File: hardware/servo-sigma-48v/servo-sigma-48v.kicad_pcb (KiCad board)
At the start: 4 copper layers, 48.7 x 68.5 mm, 154 parts, among them J1 CONN_01X02, J2 CONN_02X05, J3 CONN_01X03, J4 CONN_01X03_MALE, J6 629_105_150_921, Q1 STL160NS3LLH7, Q2 STL160NS3LLH7, Q3 STL160NS3LLH7, Q4 STL160NS3LLH7, Q5 STL160NS3LLH7, Q6 STL160NS3LLH7, U1 ST1S14, U2 TPS70950, U3 ACS711, U4 L6398, U5 STM32F411RETx, U6 L6398, U7 L6398, U8 TPS70933, U9 TSV994, Y1 ABM3-8.000MHZ-D2Y-T

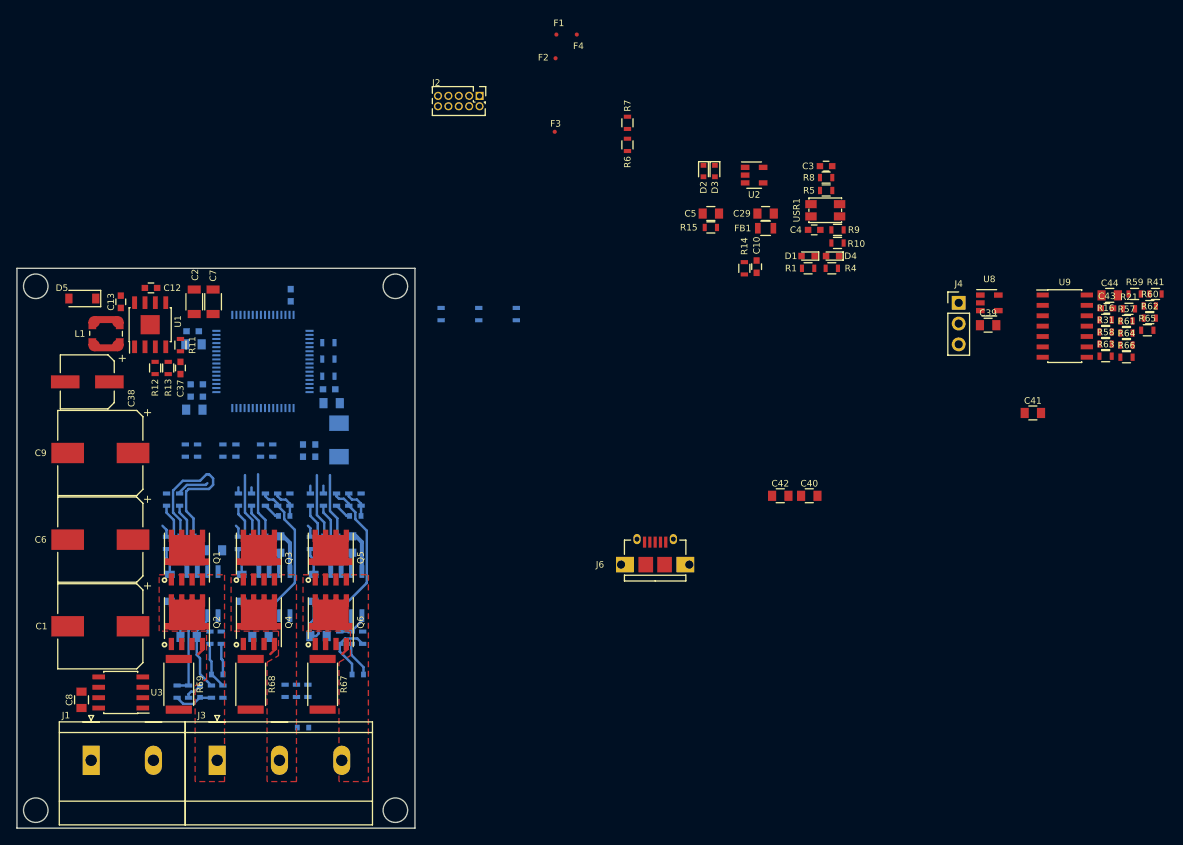
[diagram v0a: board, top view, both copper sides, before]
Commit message: Finished routing of the servo controller
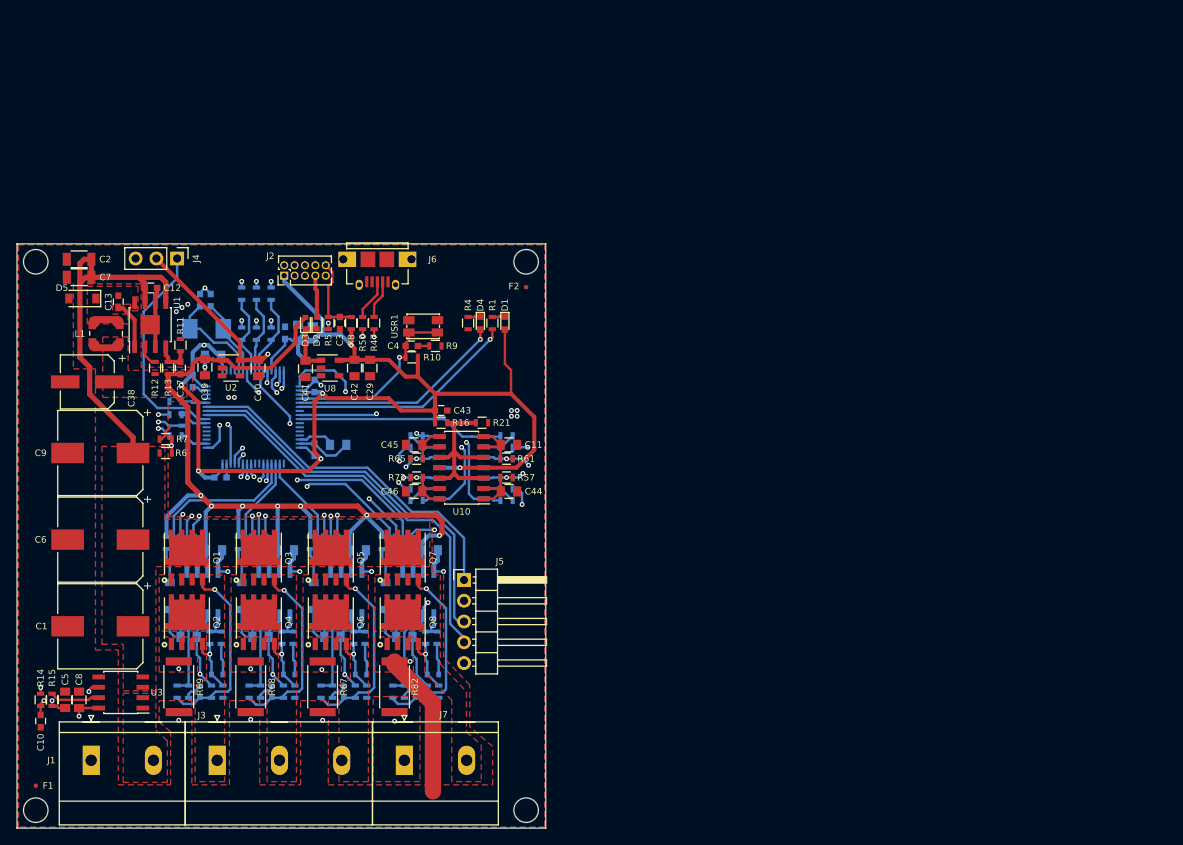
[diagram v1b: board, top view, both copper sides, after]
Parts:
- removed R17, R20, R28, R30, R38, R40: 10, Resistors_SMD:R_0603
- added C11: 4.7uF 25V, Capacitors_SMD:C_0805, F.Cu at (142.7, 74.2)
- added C45: 4.7uF 25V, Capacitors_SMD:C_0805, F.Cu at (131.1, 74.2)
- added C46: 4.7uF 25V, Capacitors_SMD:C_0805, F.Cu at (131.1, 79.9)
- added C47: 1uF 100V, Capacitors_SMD:C_0805, B.Cu at (133.0, 87.1)
- added C48: 100pF 100V, Capacitors_SMD:C_0603, B.Cu at (130.5, 86.2)
- added C49: 100pF 100V, Capacitors_SMD:C_0603, B.Cu at (128.9, 86.2)
- added C50: 1uF 100V, Capacitors_SMD:C_0805, B.Cu at (129.9, 97.7)
- added D17: STPS0560Z, Diodes_SMD:D_SOD-123, B.Cu at (127.6, 92.7)
- added D6: BAT30KFILM, Diodes_SMD:D_SOD-523, B.Cu at (131.3, 104.4)
- added D7: BAT30KFILM, Diodes_SMD:D_SOD-523, B.Cu at (133.4, 102.3)
- added J5: CONN_01X05, Pin_Headers:Pin_Header_Angled_1x05_Pitch2.54mm, F.Cu at (137.2, 90.7)
- added J7: CONN_01X02, Sigmadrone:PhoenixContact_MKDS_02x7.62mm_Vertical, F.Cu at (129.9, 112.8)
- added Q7: STL160NS3LLH7, Sigmadrone:PQFN_5x6_SGD, F.Cu at (129.7, 88.0)
- added Q8: STL160NS3LLH7, Sigmadrone:PQFN_5x6_SGD, F.Cu at (129.7, 95.9)
- added R70: 1.0k 0.1%, Resistors_SMD:R_0603, B.Cu at (142.4, 79.6)
- added R71: 1.0k 0.1%, Resistors_SMD:R_0603, B.Cu at (142.4, 78.2)
- added R72: 10k 0.1%, Resistors_SMD:R_0603, F.Cu at (131.4, 78.2)
- added R73: 10k 0.1%, Resistors_SMD:R_0603, B.Cu at (142.4, 81.0)
- added R74: 5, Resistors_SMD:R_0603, B.Cu at (129.9, 104.4)
- added R75: 5, Resistors_SMD:R_0603, B.Cu at (133.9, 97.8)
- added R76: 21, Resistors_SMD:R_0603, B.Cu at (128.5, 104.4)
- added R77: 21, Resistors_SMD:R_0603, B.Cu at (132.5, 97.8)
- added R78: 5, Resistors_SMD:R_0603, B.Cu at (127.2, 86.2)
- added R79: 10k, Resistors_SMD:R_0603, B.Cu at (132.7, 104.4)
- added R80: 10k, Resistors_SMD:R_0603, B.Cu at (134.1, 104.4)
- added R82: 0.0005 1%, Resistors_SMD:R_2512, F.Cu at (128.7, 103.8)
- added U10: OPA4374, Housings_SOIC:SOIC-14_3.9x8.7mm_Pitch1.27mm, F.Cu at (136.9, 77.0)
- added U11: L6398, Housings_SOIC:SOIC-8_3.9x4.9mm_Pitch1.27mm, B.Cu at (131.6, 92.4)
- F3, F4, FB1, R31, R41, R58, R59, R60, R62, R63, R64, R66: moved to B.Cu
- R47, R50: moved to F.Cu
- U9: value TSV994 -> OPA4374; moved to B.Cu
- moved F1 111.8 mm to (84.8, 115.9)
- moved C10 103.8 mm to (85.4, 108.0), turned to 90 degrees
- moved F3 102.1 mm to (84.8, 115.9)
- moved R14 101.0 mm to (85.4, 105.4)
- moved R15 99.2 mm to (86.8, 105.4), turned to 270 degrees
- moved C5 98.9 mm to (88.4, 105.4), turned to 270 degrees
- moved C39 96.0 mm to (105.5, 64.7), turned to 90 degrees
- moved J4 95.8 mm to (102.1, 51.4), turned to 270 degrees
- moved R41 93.2 mm to (131.4, 78.2)
- moved R60 91.6 mm to (131.4, 75.9)
- moved R62 90.9 mm to (131.4, 73.1)
- moved R65 90.8 mm to (131.4, 75.9)
- moved R59 89.8 mm to (131.4, 74.5)
- moved C41 89.2 mm to (117.8, 64.9), turned to 90 degrees
- moved R31 86.5 mm to (131.4, 79.6)
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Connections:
- C4 pad 2: /MCU/PC13 -> /MCU/PA4
- R10 pad 2: /MCU/PC13 -> /MCU/PA4
- R57 pad 1: Net-(R41-Pad2) -> Net-(R57-Pad1)
- R61 pad 1: Net-(R60-Pad2) -> Net-(R61-Pad1)
- R61 pad 2: Net-(C44-Pad2) -> Net-(C11-Pad2)
- R64 pad 2: Net-(R64-Pad2) -> Net-(R61-Pad1)
- R65 pad 1: Net-(R64-Pad2) -> Net-(R60-Pad2)
- R65 pad 2: Net-(C44-Pad2) -> Net-(C45-Pad2)
- U5 pad 17: /MCU/PA3 -> /MCU/IR_FB
- U5 pad 21: /MCU/PA5 -> /MCU/LED_WARN
- U5 pad 22: /MCU/PA6 -> /MCU/LED_STATUS
- U5 pad 34: /MCU/PB13 -> /MCU/PWM_AL
- U5 pad 35: /MCU/PB14 -> /MCU/PWM_BL
- U5 pad 36: /MCU/PB15 -> /MCU/PWM_CL
- U5 pad 37: /MCU/PC6 -> /MCU/AUX_H
- U5 pad 38: /MCU/PC7 -> /MCU/AUX_L
- U5 pad 41: /MCU/PA8 -> /MCU/PWM_AH
- U5 pad 42: /MCU/PA9 -> /MCU/PWM_BH
- U5 pad 43: /MCU/PA10 -> /MCU/PWM_CH
- U9 pad 1: Net-(C44-Pad2) -> /MCU/IA_FB
- U9 pad 10: Net-(R60-Pad2) -> Net-(R61-Pad1)
- U9 pad 12: Net-(R64-Pad2) -> Net-(R57-Pad1)
- U9 pad 13: Net-(R63-Pad2) -> Net-(R70-Pad2)
- U9 pad 14: /MCU/IC_FB -> /MCU/IR_FB
- U9 pad 2: Net-(C44-Pad2) -> Net-(R31-Pad2)
- U9 pad 3: Net-(R16-Pad1) -> Net-(R41-Pad2)
- U9 pad 4: +5V -> +3V3
- U9 pad 5: Net-(R41-Pad2) -> Net-(R60-Pad2)
- U9 pad 6: Net-(R31-Pad2) -> Net-(R59-Pad2)
- U9 pad 7: /MCU/IA_FB -> /MCU/IB_FB
- U9 pad 8: /MCU/IB_FB -> /MCU/IC_FB
- U9 pad 9: Net-(R59-Pad2) -> Net-(R63-Pad2)
- USR1 pad 2: /MCU/PC13 -> /MCU/PA4
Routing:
- net GND: track 64.4 -> 276.0 mm, vias 0 -> 36
- net +3V3: track 7.49 -> 197.6 mm, vias 0 -> 9
- net +15V: track 9.13 -> 121.2 mm, vias 0 -> 7
- net /MOSFETs/C_ISENSE_P: track 0.00 -> 64.6 mm, vias 0 -> 2
- net /MOSFETs/PHASE_B: track 0.00 -> 64.3 mm, vias 0 -> 2
- net /MOSFETs/PHASE_A: track 4.98 -> 68.9 mm, vias 0 -> 2
- net +5V: track 0.00 -> 60.5 mm, vias 0 -> 1
- net /MCU/CURRENT_FAULT: track 0.00 -> 58.6 mm, vias 0 -> 3
- net /MCU/CURRENT_ADC: track 0.00 -> 54.6 mm, vias 0 -> 2
- net /MOSFETs/PHASE_C: track 9.85 -> 59.5 mm, vias 0 -> 2
- net /MCU/ENCODER_Z: track 0.00 -> 49.6 mm
- net /MCU/ENCODER_A: track 0.00 -> 48.1 mm
- net +BATT: track 0.00 -> 46.7 mm
- net /MCU/ENCODER_B: track 0.00 -> 43.3 mm
- net /MOSFETs/R_ISENSE_P: track 0.00 -> 41.9 mm, vias 0 -> 2
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- added copper zone on F.Cu, net +15V
- added copper zone on F.Cu, net +BATT
- added copper zone on F.Cu, net /MOSFETs/A_ISENSE_P
- added copper zone on F.Cu, net /MOSFETs/B_ISENSE_P
- added copper zone on F.Cu, net /MOSFETs/C_ISENSE_P
- added copper zone on F.Cu, net /MOSFETs/PHASE_R
- added copper zone on F.Cu, net /MOSFETs/R_ISENSE_P
- added copper zone on B.Cu, net GND
- added copper zone on F.Cu, net GND
- added copper zone on In1.Cu, net GND
- added copper zone on F.Cu, net Net-(C13-Pad2)
- added copper zone on F.Cu, net VIN
- removed copper zone on In2.Cu, net GND
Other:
- board size 48.7 x 68.5 mm -> 64.7 x 71.5 mm

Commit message: Fixed overlapping footprints
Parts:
- moved U3 0.20 mm to (95.2, 104.7)
- moved C1 0.20 mm to (92.7, 96.6)
- moved C6 0.10 mm to (92.7, 85.9)
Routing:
- net Net-(D16-Pad2): track 23.1 -> 24.9 mm
- net Net-(D13-Pad2): track 23.0 -> 24.8 mm
- net Net-(D10-Pad2): track 23.3 -> 24.8 mm
- net /MOSFETs/PHASE_A: track 68.9 -> 70.1 mm, vias 2 -> 10
- net /MOSFETs/PHASE_B: track 64.3 -> 65.0 mm, vias 2 -> 10
- net /MOSFETs/PHASE_C: vias 2 -> 10
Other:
- board size 64.7 x 71.5 mm -> 64.7 x 71.7 mm

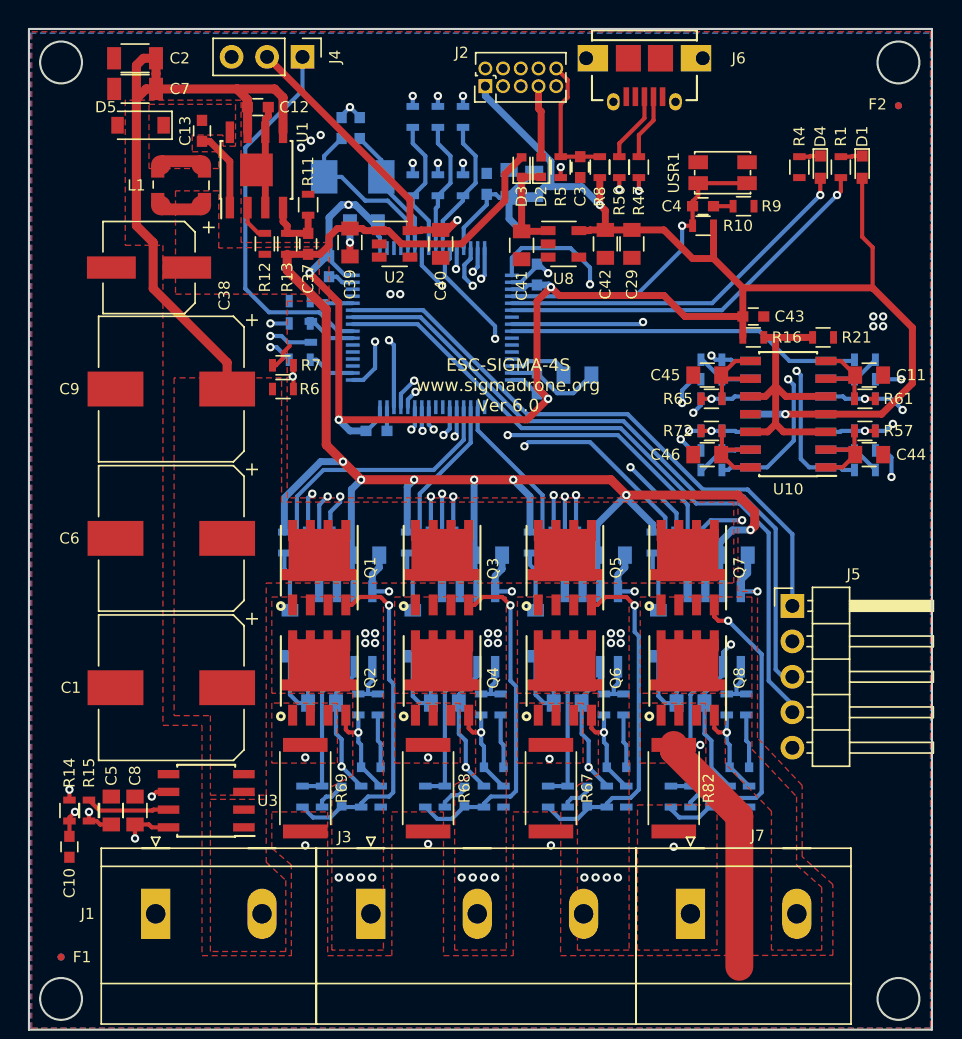
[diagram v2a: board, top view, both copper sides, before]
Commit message: Updated the footprints
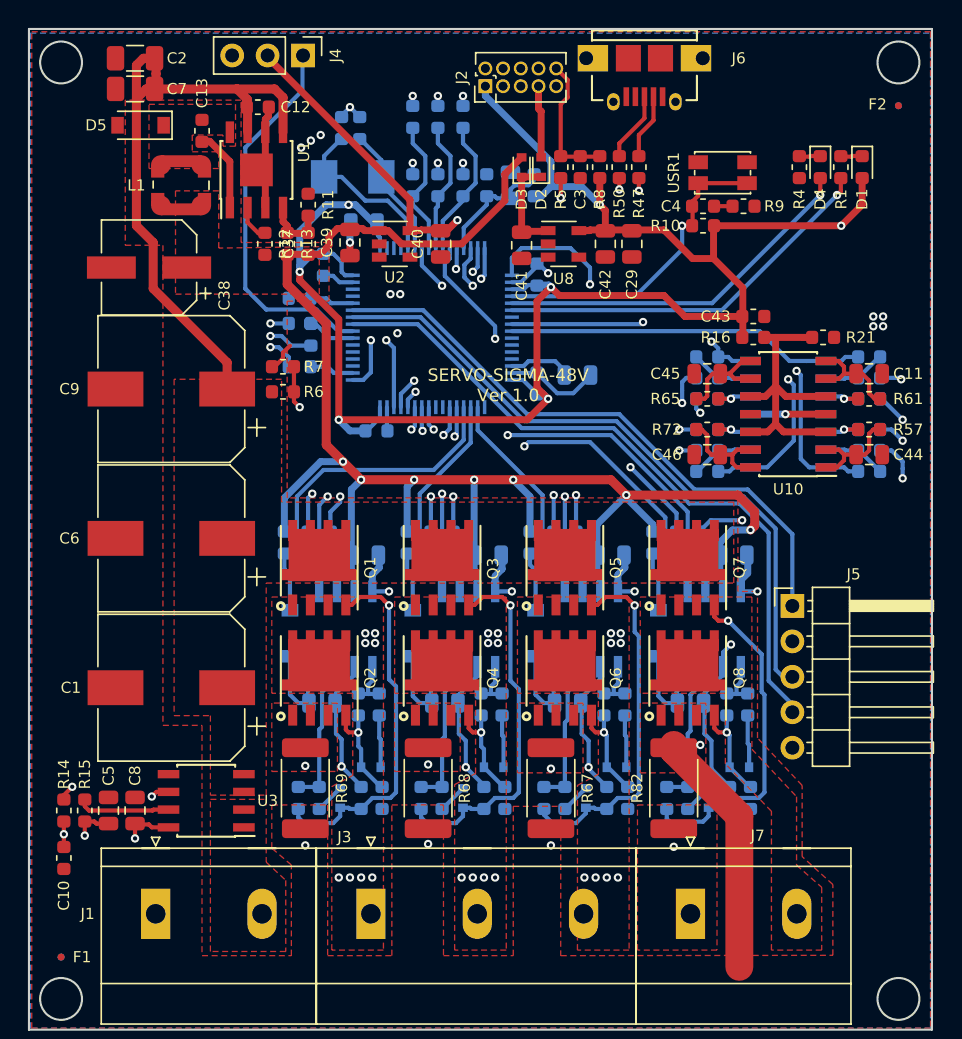
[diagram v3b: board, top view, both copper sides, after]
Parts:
- C1, C6, C9: footprint Capacitors_SMD:CP_Elec_10x10 -> Capacitor_SMD:CP_Elec_10x10
- C10, C12, C13, C14, C16, C18, C19, C21, C23, C24, C25, C27, C3, C30, C32, C33, C35, C37, C4, C43, C48, C49: footprint Capacitors_SMD:C_0603 -> Capacitor_SMD:C_0603_1608Metric
- C11, C15, C17, C20, C22, C26, C28, C29, C31, C34, C36, C39, C40, C41, C42, C44, C45, C46, C47, C5, C50, C8: footprint Capacitors_SMD:C_0805 -> Capacitor_SMD:C_0805_2012Metric
- C2, C7: footprint Capacitors_SMD:C_1206 -> Capacitor_SMD:C_1206_3216Metric
- C38: footprint Capacitors_SMD:CP_Elec_6.3x7.7 -> Capacitor_SMD:CP_Elec_6.3x7.7
- D1, D4: footprint LEDs:LED_0603 -> LED_SMD:LED_0603_1608Metric
- FB1: footprint Resistors_SMD:R_0805 -> Resistor_SMD:R_0603_1608Metric
- J2: footprint Pin_Headers:Pin_Header_Straight_2x05_Pitch1.27mm -> Connector_PinHeader_1.27mm:PinHeader_2x05_P1.27mm_Vertical
- J4: footprint Pin_Headers:Pin_Header_Straight_1x03_Pitch2.54mm -> Connector_PinHeader_2.54mm:PinHeader_1x03_P2.54mm_Vertical
- J5: footprint Pin_Headers:Pin_Header_Angled_1x05_Pitch2.54mm -> Connector_PinHeader_2.54mm:PinHeader_1x05_P2.54mm_Horizontal
- L1: footprint Inductors_SMD:L_Wuerth_WE-TPC-3816 -> Inductor_SMD:L_Wuerth_WE-TPC-3816
- R1, R10, R11, R12, R13, R14, R15, R16, R18, R19, R2, R21, R22, R23, R24, R25, R26, R27, R29, R3, R31, R32, R33, R34, R35, R36, R37, R39, R4, R41, R42, R43, R44, R45, R46, R47, R48, R49, R5, R50, R51, R52, R53, R54, R55, R56, R57, R58, R59, R6, R60, R61, R62, R63, R64, R65, R66, R7, R70, R71, R72, R73, R74, R75, R76, R77, R78, R79, R8, R80, R9: footprint Resistors_SMD:R_0603 -> Resistor_SMD:R_0603_1608Metric
- R67, R68, R69, R82: footprint Resistors_SMD:R_2512 -> Resistor_SMD:R_2512_6332Metric
- U1: footprint Housings_SOIC:SOIC-8-1EP_3.9x4.9mm_Pitch1.27mm -> Package_SO:SOIC-8-1EP_3.9x4.9mm_P1.27mm_EP2.35x2.35mm
- U10, U9: footprint Housings_SOIC:SOIC-14_3.9x8.7mm_Pitch1.27mm -> Package_SO:SOIC-14_3.9x8.7mm_P1.27mm
- U11, U3, U4, U6, U7: footprint Housings_SOIC:SOIC-8_3.9x4.9mm_Pitch1.27mm -> Package_SO:SOIC-8_3.9x4.9mm_P1.27mm
- U2, U8: footprint TO_SOT_Packages_SMD:SOT-23-5 -> Package_TO_SOT_SMD:SOT-23-5
- U5: footprint Housings_QFP:LQFP-64_10x10mm_Pitch0.5mm -> Package_QFP:LQFP-64_10x10mm_P0.5mm
- Y1: footprint Crystals:Crystal_SMD_Abracon_ABM3-2pin_5.0x3.2mm -> Crystal:Crystal_SMD_Abracon_ABM3-2Pin_5.0x3.2mm
- moved C10 0.89 mm to (85.0, 108.8)
- moved R3 0.50 mm to (101.9, 73.6)
- moved C24 0.41 mm to (103.6, 66.3)
- moved R14 0.40 mm to (85.0, 105.4)
- moved R62 0.36 mm to (131.1, 72.9)
- moved R66 0.36 mm to (142.7, 72.9)
- moved R41 0.32 mm to (131.1, 78.1)
- moved R72 0.32 mm to (131.1, 78.1), turned to 180 degrees
- moved R34 0.32 mm to (110.6, 104.5)
- moved R58 0.32 mm to (131.1, 81.1)
- moved R59 0.32 mm to (131.1, 74.4)
- moved R76 0.32 mm to (128.2, 104.5)
- moved R24 0.32 mm to (101.8, 104.5)
- moved R53 0.32 mm to (119.4, 104.5)
- moved R57 0.32 mm to (142.7, 78.1), turned to 0 degrees
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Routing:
- net +3V3: track 197.6 -> 206.3 mm, vias 9 -> 10
- net /MCU/CURRENT_ADC: track 54.6 -> 56.8 mm
- net /MCU/VBAT_ADC: track 20.1 -> 22.1 mm
- net Net-(C30-Pad1): track 11.1 -> 9.17 mm
- net /MCU/CURRENT_FAULT: track 58.4 -> 60.2 mm
- net Net-(D10-Pad2): track 24.8 -> 26.3 mm
- net Net-(D13-Pad2): track 24.8 -> 26.2 mm
- net Net-(D6-Pad2): track 23.1 -> 24.4 mm
- net GND: track 276.0 -> 277.2 mm, vias 36 -> 37
- net /MOSFETs/R_ISENSE_P: track 41.9 -> 43.1 mm
- net Net-(C46-Pad2): track 6.45 -> 7.53 mm
- net Net-(C44-Pad2): track 6.46 -> 7.40 mm
- net Net-(C45-Pad2): track 6.45 -> 7.36 mm
- net Net-(D16-Pad2): track 24.9 -> 25.8 mm
- net Net-(C11-Pad2): track 6.94 -> 7.77 mm
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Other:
- board text added: "SERVO-SIGMA-48V Ver 1.0"
- board text removed: "ESC-SIGMA-4S www.sigmadrone.org Ver 6.0"
